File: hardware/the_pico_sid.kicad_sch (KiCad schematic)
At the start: 19 parts, among them J1 SWD, U1 TL084, U2 SID_6581, U3 Pico, U4 4050, U5 4050, U6 4050

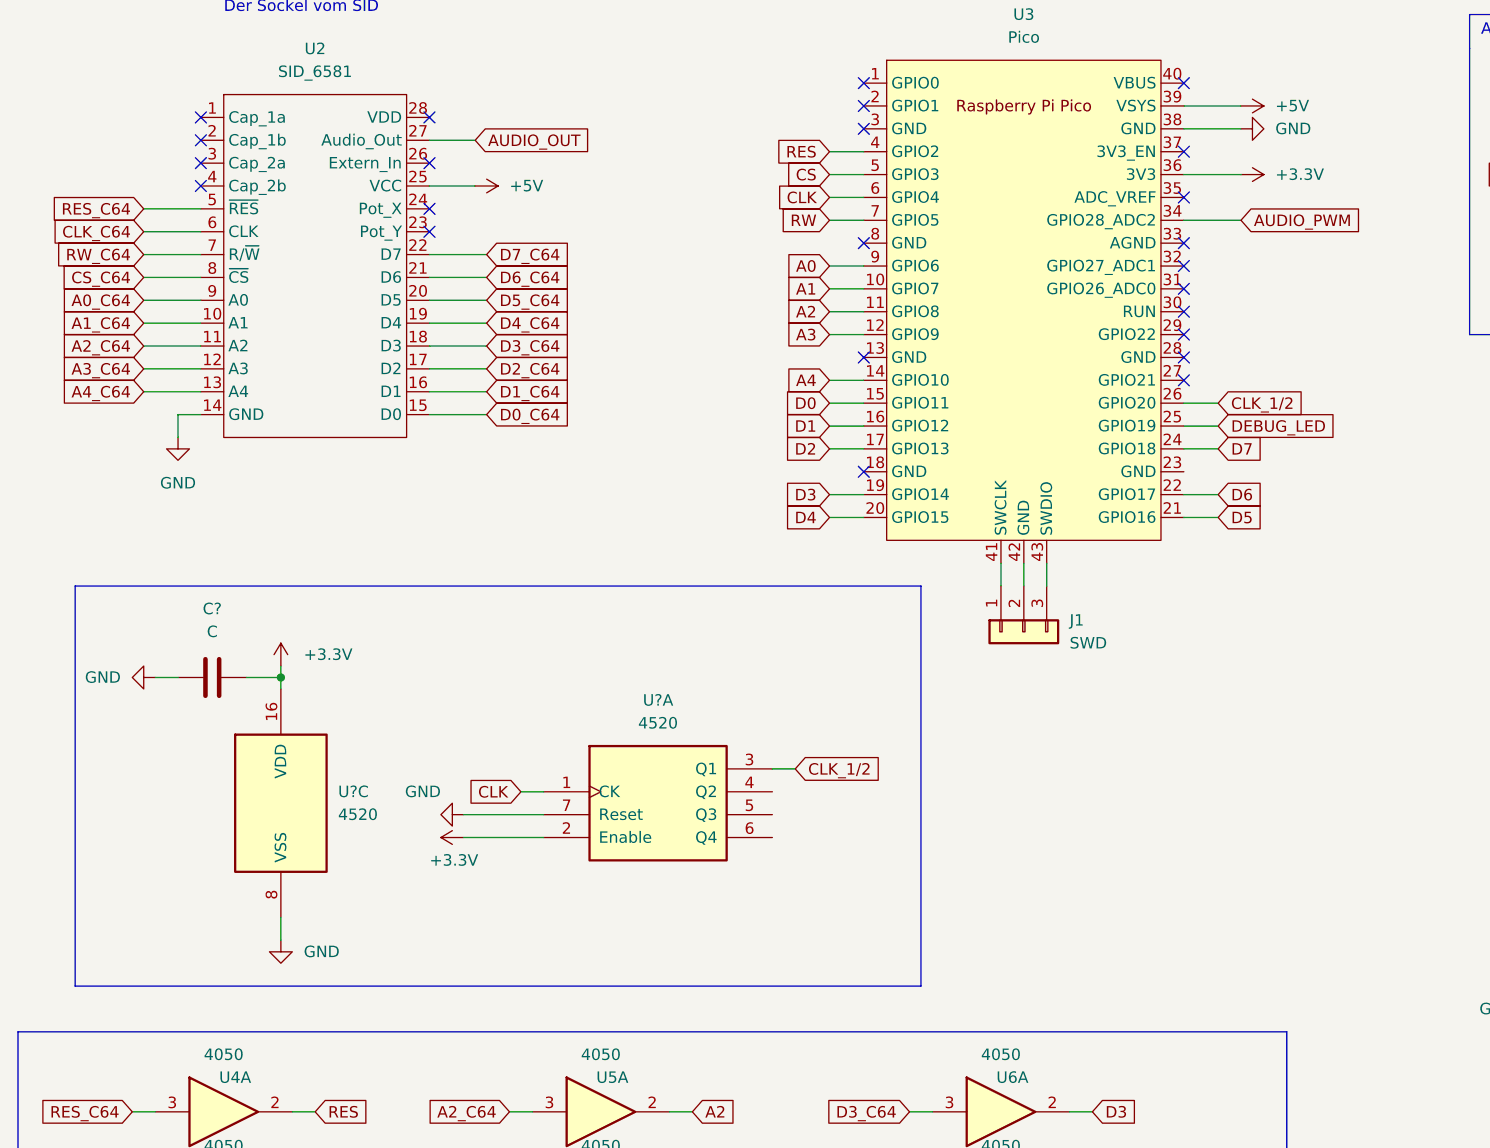
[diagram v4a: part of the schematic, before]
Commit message: schematic: change pin clk with cs, remove counters
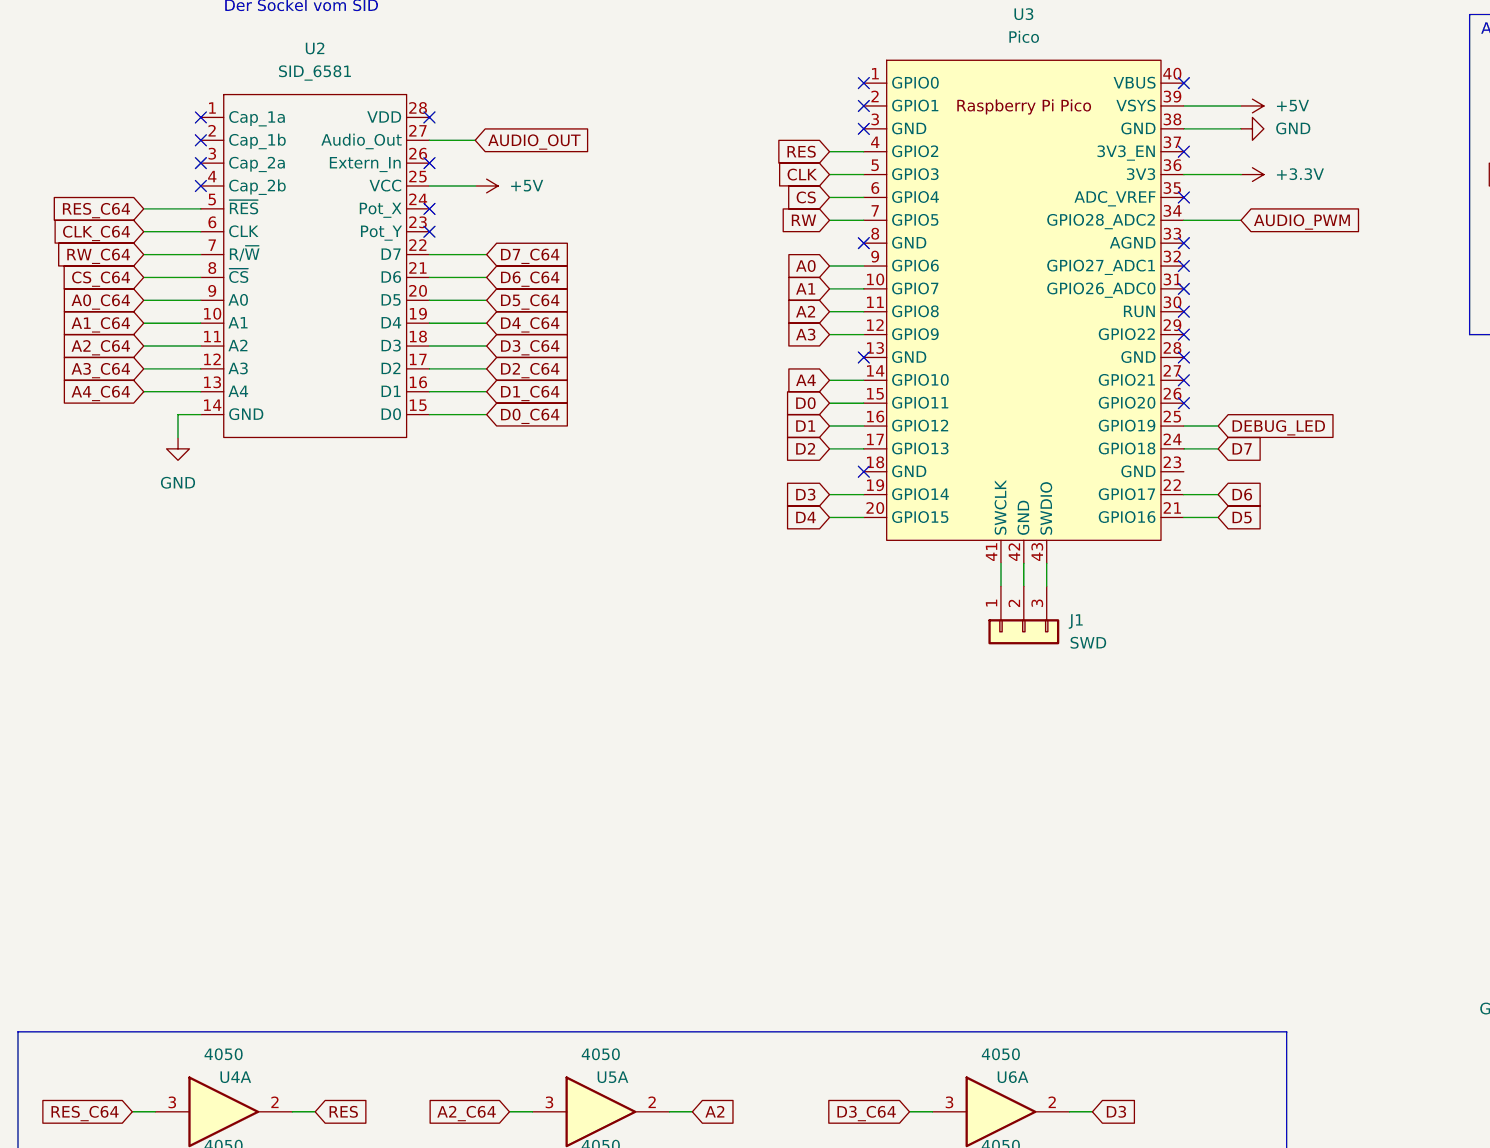
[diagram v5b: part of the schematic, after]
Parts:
- removed C?: C, symbol Device:C
- removed U? (x2): 4520, symbol 4xxx:4520
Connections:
- net CLK: now also U3.5 (GPIO3); no longer U3.6 (GPIO4)
- net CS: now also U3.6 (GPIO4); no longer U3.5 (GPIO3)
- net CLK_1/2: no longer names the net of U3.26 (GPIO20)
- no-connect marks 26 -> 27

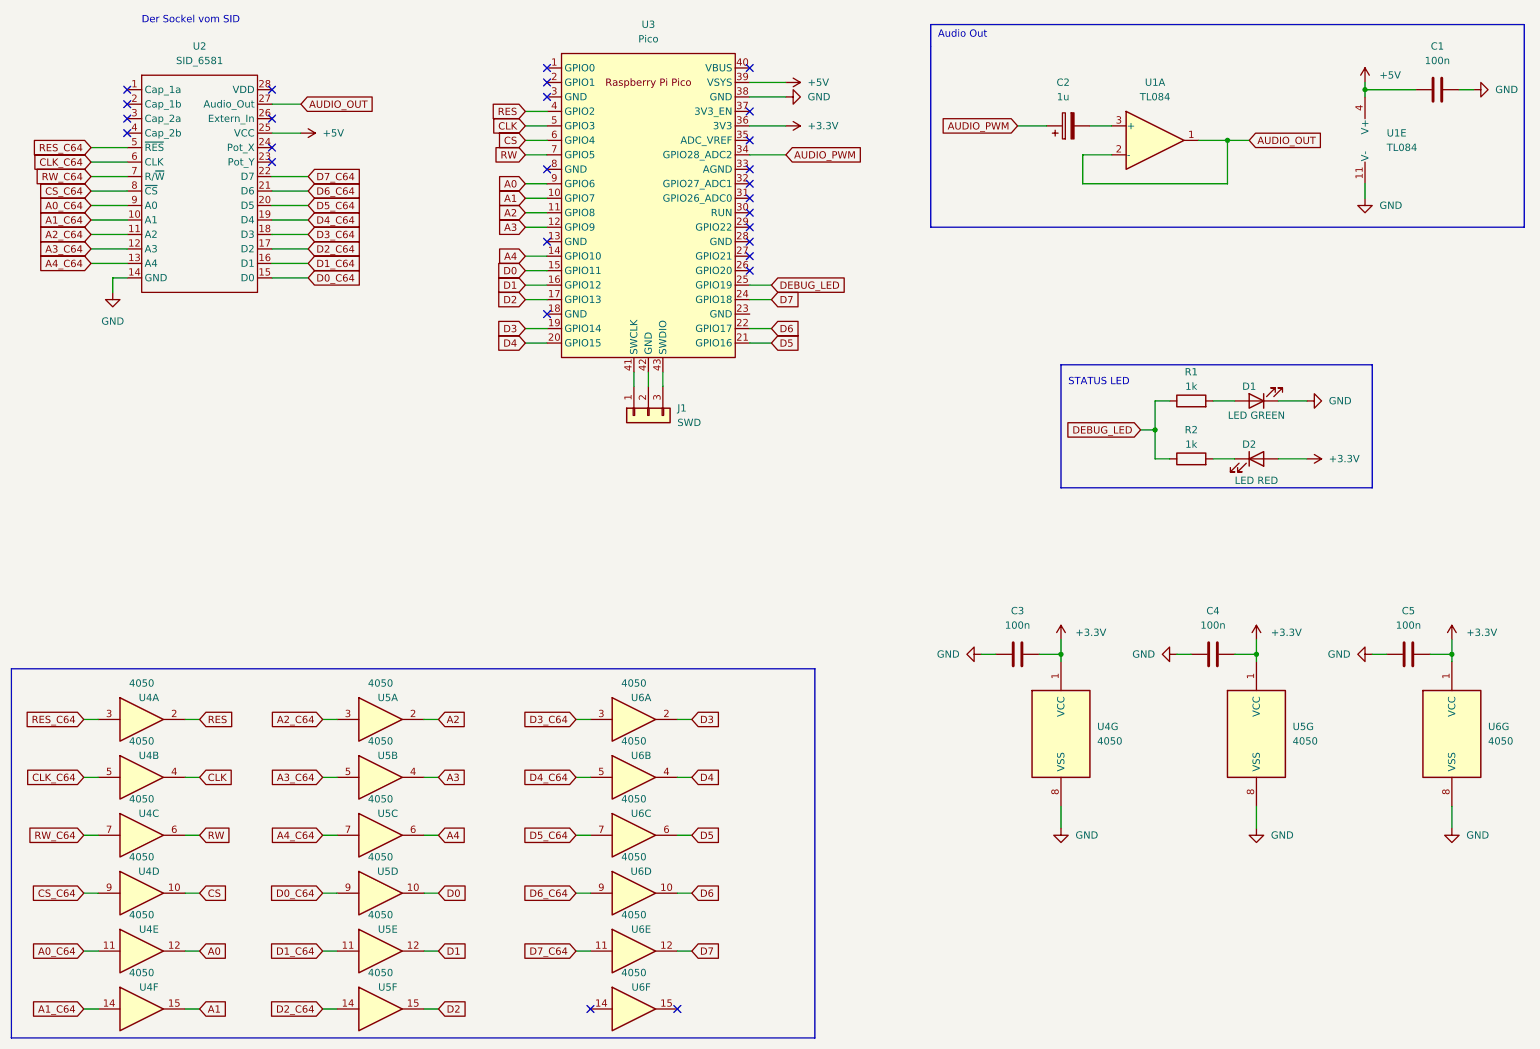
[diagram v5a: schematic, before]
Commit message: schematic: one 74hc4050 changed to 74hc245 for bidirection data
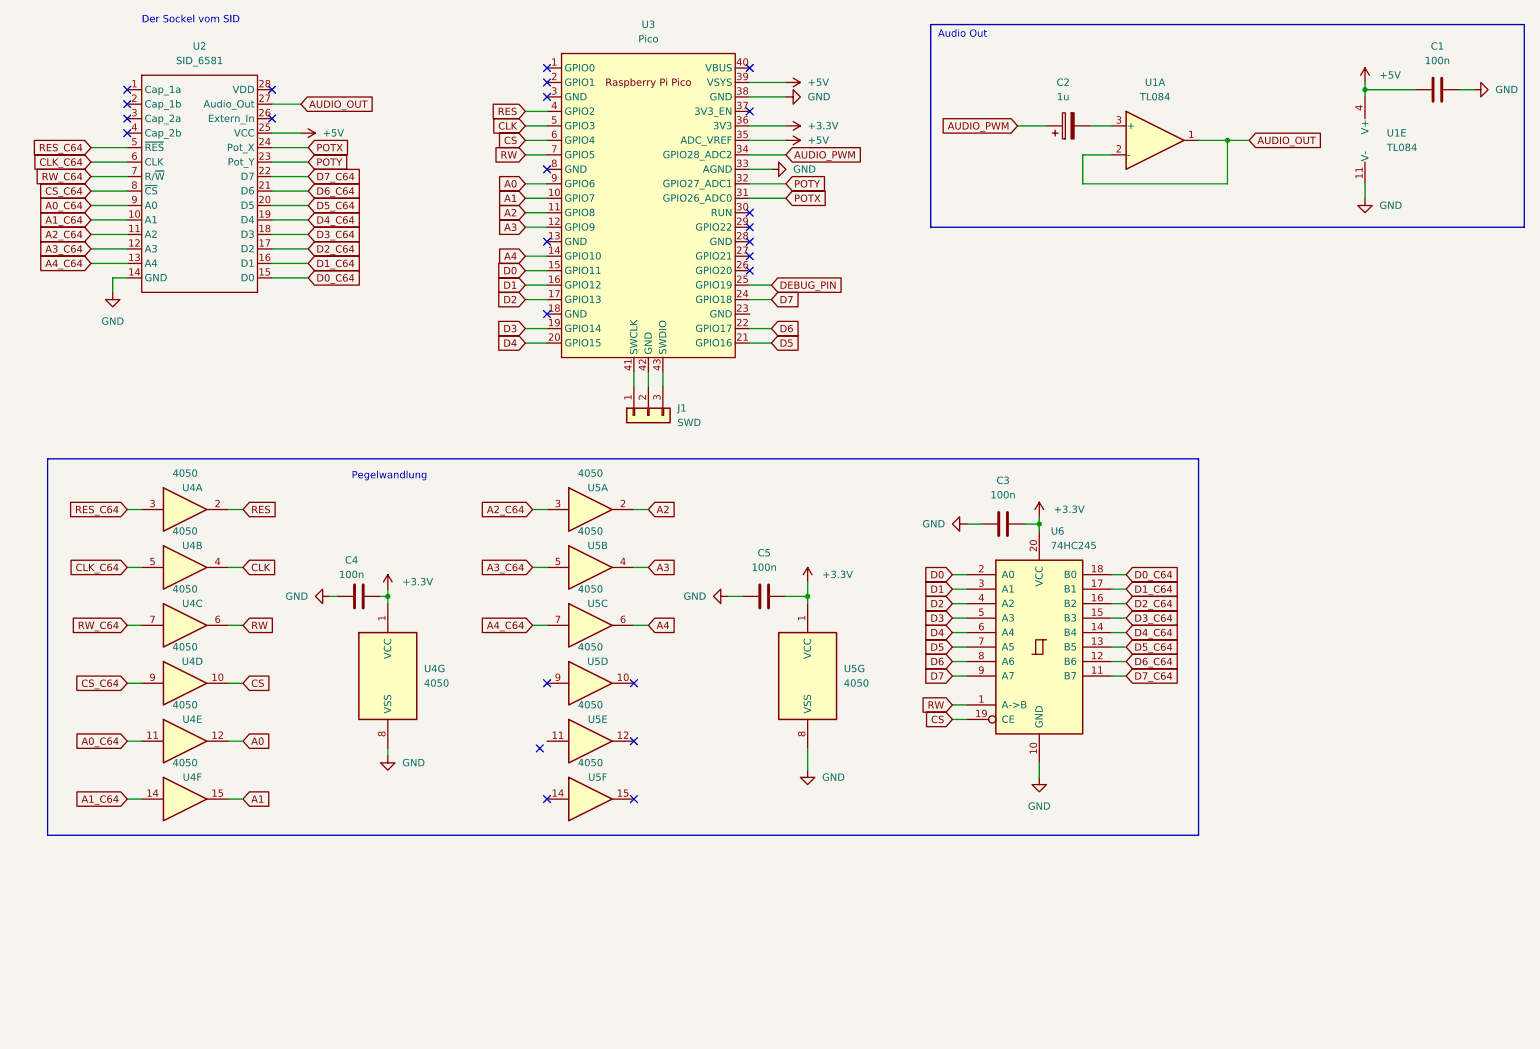
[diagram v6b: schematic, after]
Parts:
- removed C5: 100n, symbol Device:C
- removed D1: LED GREEN, symbol Device:LED
- removed D2: LED RED, symbol Device:LED
- removed R1, R2: 1k, symbol Device:R
- removed U6: 4050, symbol 4xxx:4050
- added C3: 100n, symbol Device:C
- added U6: 74HC245, symbol 74xx:74HC245
- renumbered C3 to C4, C4 to C5
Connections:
- net +3.3V: now also C3.2, U6.20 (VCC)
- net +5V: now also U3.35 (ADC_VREF)
- net CS: now also U6.19 (CE)
- net D0: now also U6.2 (A0); no longer U5.10
- net D0_C64: now also U6.18 (B0); no longer U5.9
- net D1: now also U6.3 (A1); no longer U5.12
- net D1_C64: now also U6.17 (B1); no longer U5.11
- net D2: now also U6.4 (A2); no longer U5.15
- net D2_C64: now also U6.16 (B2); no longer U5.14
- net D3: now also U6.5 (A3)
- net D3_C64: now also U6.15 (B3)
- net D4: now also U6.6 (A4)
- net D4_C64: now also U6.14 (B4)
- net D5: now also U6.7 (A5)
- net D5_C64: now also U6.13 (B5)
- net D6: now also U6.8 (A6)
- net D6_C64: now also U6.12 (B6)
- net D7: now also U6.9 (A7)
- net D7_C64: now also U6.11 (B7)
- net GND: now also U3.33 (AGND), C3.1, U6.10 (GND)
- net RW: now also U6.1 (A->B)
- net POTX: now reaches U3.31 (GPIO26_ADC0)
- net POTX: now also U2.24 (Pot_X)
- net POTY: now reaches U3.32 (GPIO27_ADC1)
- net POTY: now also U2.23 (Pot_Y)
- net DEBUG_LED renamed DEBUG_PIN
- no-connect marks 27 -> 25
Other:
- note added: "Pegelwandlung"
- note removed: "STATUS LED"
- title: The Pico SID -> ThePicoSID
- moved on the sheet: C4, C5, U4A, U4B, U4C, U4D, U4E, U4F, U4G, U5A, U5B, U5C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

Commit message: schematic: added adc
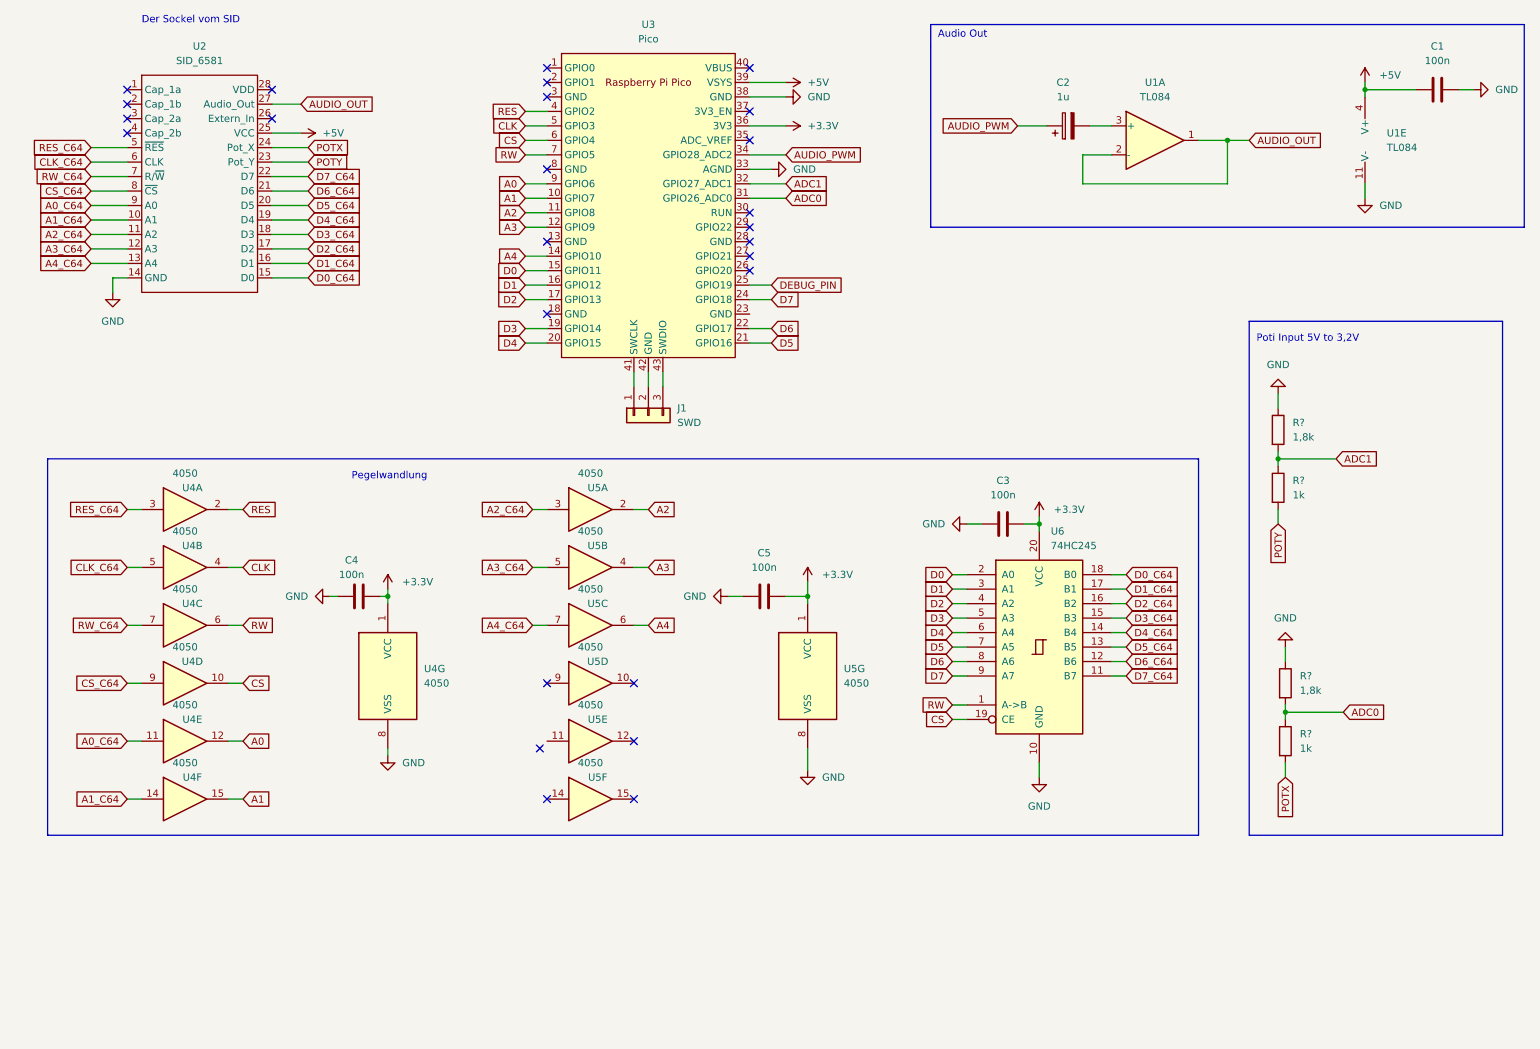
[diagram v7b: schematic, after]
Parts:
- added R? (x2): 1,8k, symbol Device:R
- added R? (x2): 1k, symbol Device:R
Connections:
- net +5V: no longer U3.35 (ADC_VREF)
- net GND: now also R?.1, R?.1
- net POTX: now also R?.2; no longer U3.31 (GPIO26_ADC0)
- net POTY: now also R?.2; no longer U3.32 (GPIO27_ADC1)
- new net ADC0: R?.1, R?.2, U3.31 (GPIO26_ADC0)
- new net ADC1: R?.1, R?.2, U3.32 (GPIO27_ADC1)
- no-connect marks 25 -> 26
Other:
- note added: "Poti Input 5V to 3,2V"
